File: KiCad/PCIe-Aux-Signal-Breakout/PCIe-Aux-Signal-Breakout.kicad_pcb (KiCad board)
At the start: 2 copper layers, 65.3 x 64.4 mm, 8 parts, among them J1 PCIexpress_x1, J2 PCIexpress_bracket, J3 Conn_02x10_Odd_Even, U1 MIC2876-5.0

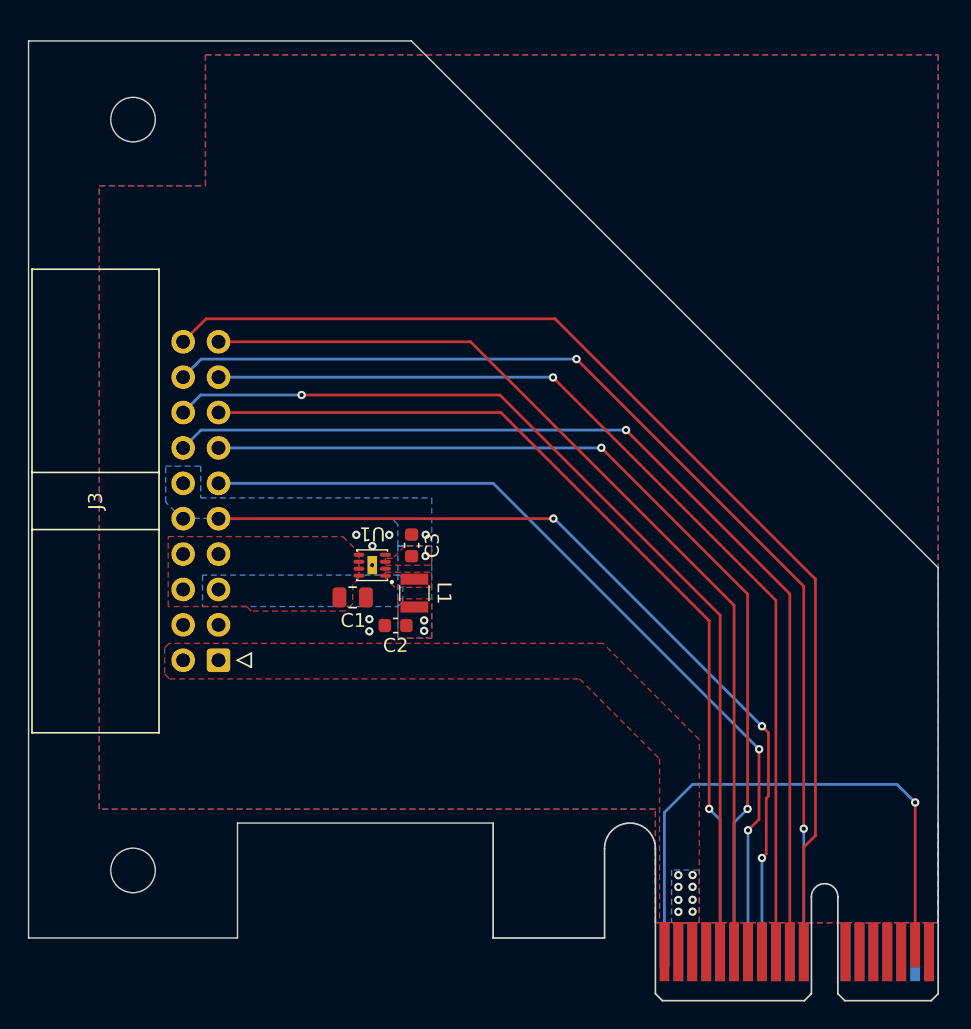
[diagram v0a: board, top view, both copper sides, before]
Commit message: finished v1.0 design
finished v1.0 pcb

added low and standard profile pcie bracket with custom connector cutout

made gerber files

added instruction files

added images of the board

added BOM
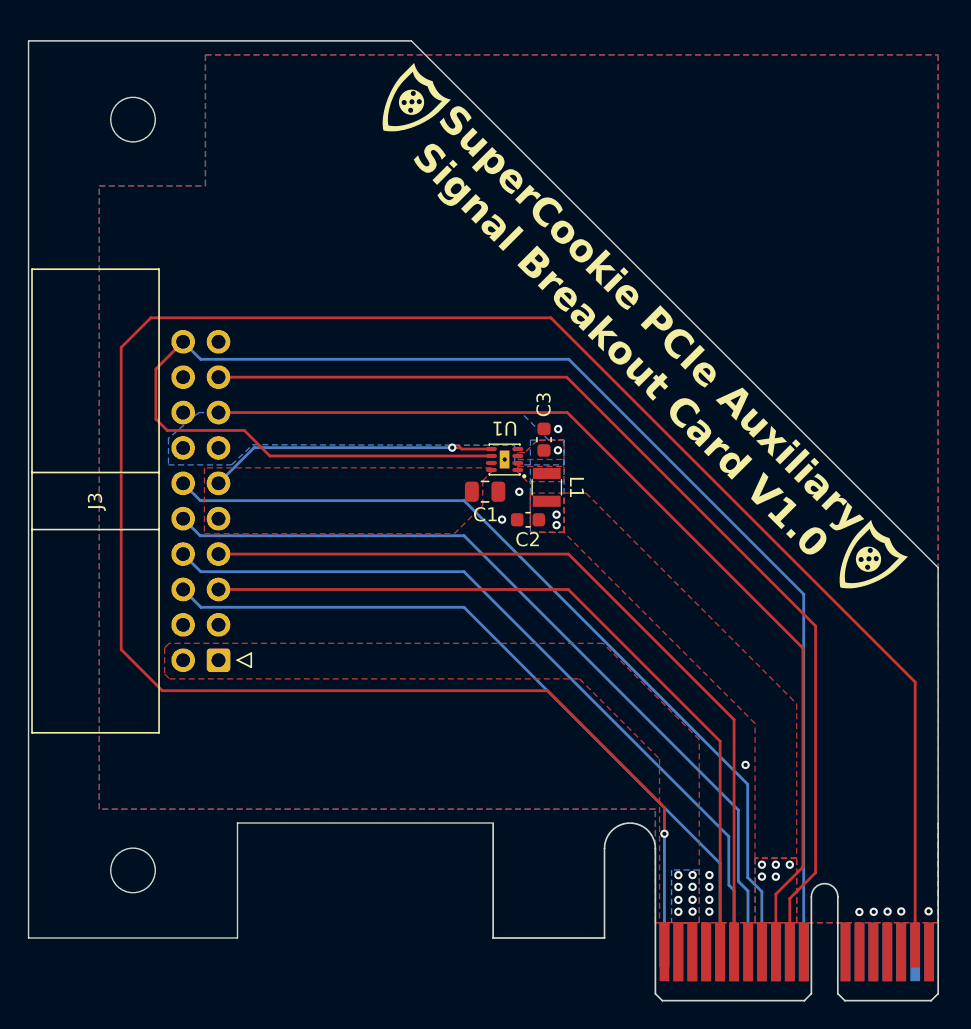
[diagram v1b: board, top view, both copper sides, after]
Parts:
- added G***: LOGO, LOGO, F.Cu at (73.5, 76.4)
- added G***: LOGO, LOGO, F.Cu at (106.3, 109.2)
- moved C3 12.2 mm to (83.2, 100.3)
- moved U1 12.2 mm to (80.4, 101.8)
- moved C1 12.2 mm to (79.0, 104.1)
- moved C2 12.2 mm to (82.1, 106.1)
- moved L1 12.2 mm to (83.4, 103.8)
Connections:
- J1 pad B11: WAKE# -> unconnected-(J1-WAKE#-PadB11)
- J3 pad 10: GND -> TDO
- J3 pad 11: TDO -> +5V
- J3 pad 12: +3.3V -> TMS
- J3 pad 13: TDI -> +3.3V
- J3 pad 14: +3.3VAUX -> +3.3V
- J3 pad 15: TCK -> TRST#
- J3 pad 16: SMBCLK -> GND
- J3 pad 17: TRST# -> +3.3VAUX
- J3 pad 18: PERST# -> GND
- J3 pad 19: SMBDAT -> GND
- J3 pad 20: WAKE# -> PERST#
- J3 pad 5: +3.3V -> SMBCLK
- J3 pad 6: +5V -> TCK
- J3 pad 7: GND -> SMBDAT
- J3 pad 8: +5V -> TDI
- J3 pad 9: TMS -> +5V
- U1 pad 6: 5VEN -> PERST#
- U1 pad 7: ~{5VPG} -> GND
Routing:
- net PRSNT: track 39.1 -> 162.8 mm
- net WAKE#: track 80.9 -> 0.00 mm
- net PERST#: track 78.1 -> 109.3 mm, vias 2 -> 0
- net +5V: track 0.00 -> 20.7 mm, vias 0 -> 1
- net SMBCLK: track 69.8 -> 55.6 mm, vias 1 -> 0
- net TDI: track 68.4 -> 56.0 mm, vias 2 -> 0
- net TCK: track 65.5 -> 53.1 mm, vias 1 -> 0
- net SMBDAT: track 69.7 -> 58.6 mm
- net TDO: track 61.6 -> 59.0 mm, vias 2 -> 0
- net TRST#: track 71.9 -> 71.6 mm, vias 1 -> 0
- net +3.3VAUX: track 74.7 -> 74.4 mm, vias 1 -> 0
- net TMS: track 61.8 -> 61.9 mm, vias 3 -> 0
- net GND: vias 6 -> 13
- net +3.3V: vias 3 -> 8
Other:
- board text added: "SuperCookie PCIe Auxiliary Signal Breakout Card V1.0"

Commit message: Added Schematic and 3D printing files
-updated board silkscreen

-added STL files for pcie brackets

-added 3d model folder for assembled boards
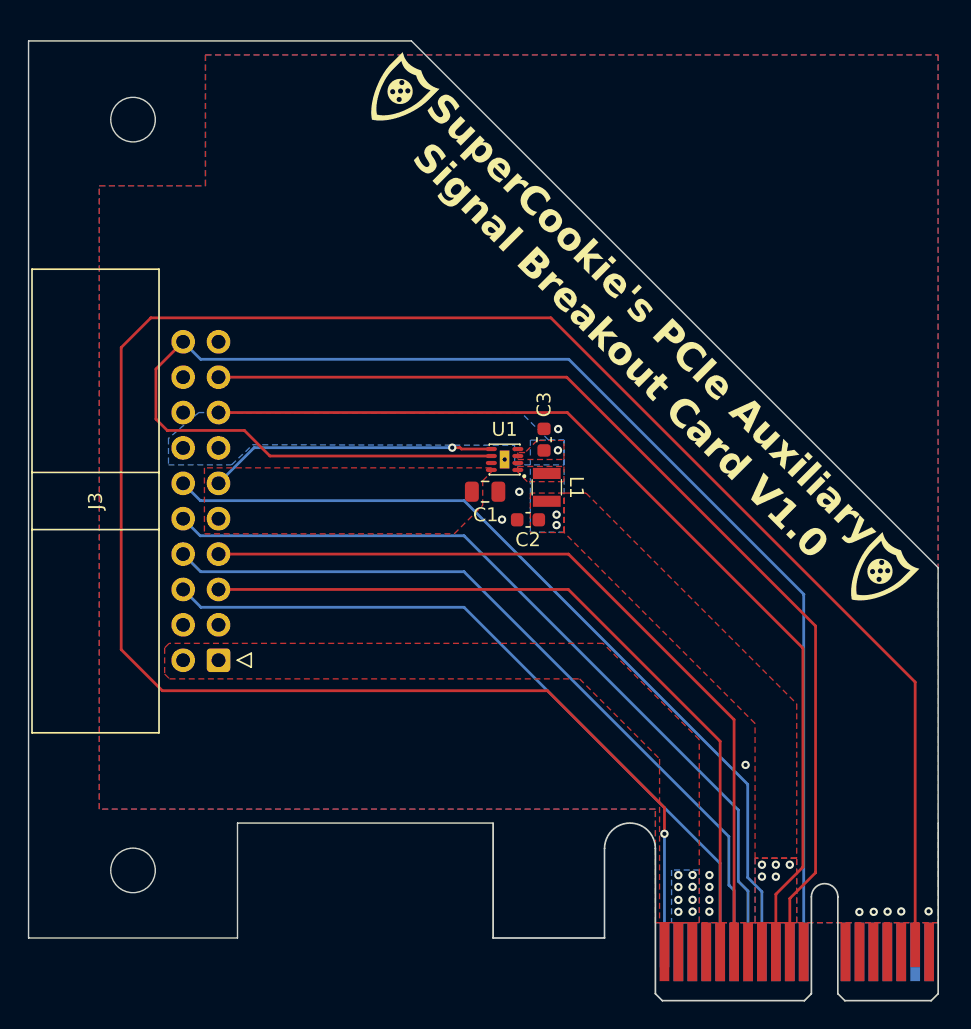
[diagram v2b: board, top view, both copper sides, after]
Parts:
- moved G*** 1.19 mm to (107.1, 110.1)
- moved G*** 1.13 mm to (72.7, 75.6)
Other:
- board text added: "SuperCookie's PCIe Auxiliary Signal Breakout Card V1.0"
- board text removed: "SuperCookie PCIe Auxiliary Signal Breakout Card V1.0"
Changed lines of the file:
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@@
 			(outputformat 1)
 			(mirror no)
-			(drillshape 1)
+			(drillshape 0)
 			(scaleselection 1)
 			(outputdirectory "")
@@
 		(at 80.415 101.77 180)
 		(property "Reference" "U1"
-			(at -0.01 2.25 180)
+			(at 0 2.165 0)
 			(unlocked yes)
 			(layer "F.SilkS")
@@
 		)
 		(fp_text user "${REFERENCE}"
-			(at 0 2.5 180)
+			(at 0 2.165 0)
 			(unlocked yes)
 			(layer "F.Fab")
@@
 	(footprint "LOGO"
 		(layer "F.Cu")
-		(at 73.483391 76.382822 -45)
+		(at 72.66138 75.60581 -45)
 		(property "Reference" "G***"
 			(at 0 0 135)
@@
 	(footprint "LOGO"
 		(layer "F.Cu")
-		(at 106.28961 109.189041 -45)
+		(at 107.111623 110.056053 -45)
 		(property "Reference" "G***"
 			(at 0 0 135)
@@
 		(layer "Edge.Cuts")
 	)
-	(gr_text "SuperCookie PCIe Auxiliary\nSignal Breakout Card V1.0"
-		(at 89.885 92.785 315)
+	(gr_text "SuperCookie's PCIe Auxiliary\nSignal Breakout Card V1.0"
+		(at 89.885 92.83 315)
 		(layer "F.SilkS")
 		(effects
